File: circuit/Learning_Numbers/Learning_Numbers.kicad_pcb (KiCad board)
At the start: 2 copper layers, 141 x 123.3 mm, 109 parts, among them SW1 SW_DIP_x01, SW10 SW_Push, SW11 SW_Push, SW12 SW_Push, SW13 SW_Push, SW14 SW_Push, SW15 SW_Push, SW16 SW_Push, SW17 SW_Push, SW18 SW_Push, SW19 SW_Push, SW2 SW_Push, SW20 SW_Push, SW21 SW_Push, SW22 SW_Push, SW23 SW_Push, SW3 SW_Push, SW4 SW_Push, SW5 SW_Push, SW6 SW_Push, SW7 SW_Push, SW8 SW_Push, SW9 SW_Push, U1 ATmega168PA-P, U2 74HC165, U3 74HC165, U4 74HC595, U5 74HC595, U6 74HC595, U7 74HC595, U8 74HC595, Y1 8Mhz

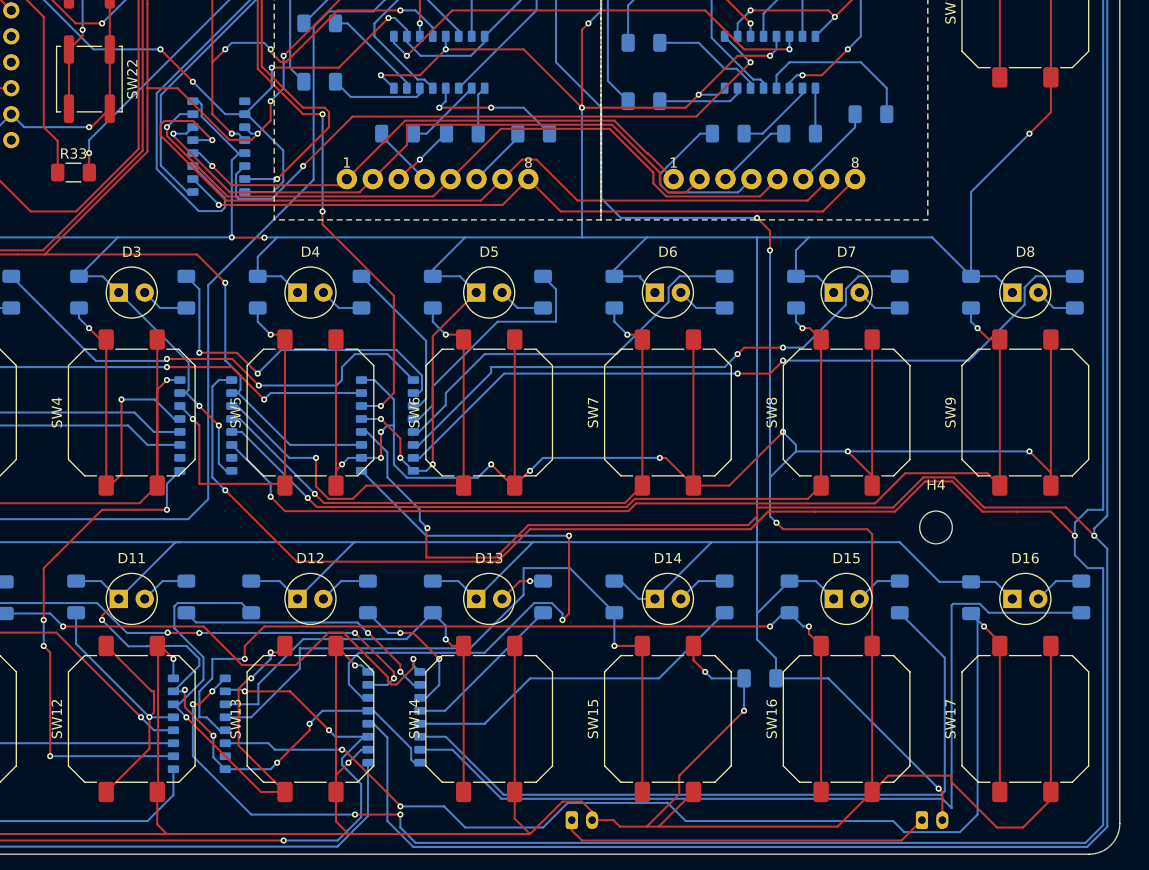
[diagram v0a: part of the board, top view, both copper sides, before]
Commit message: update pcb silk layer
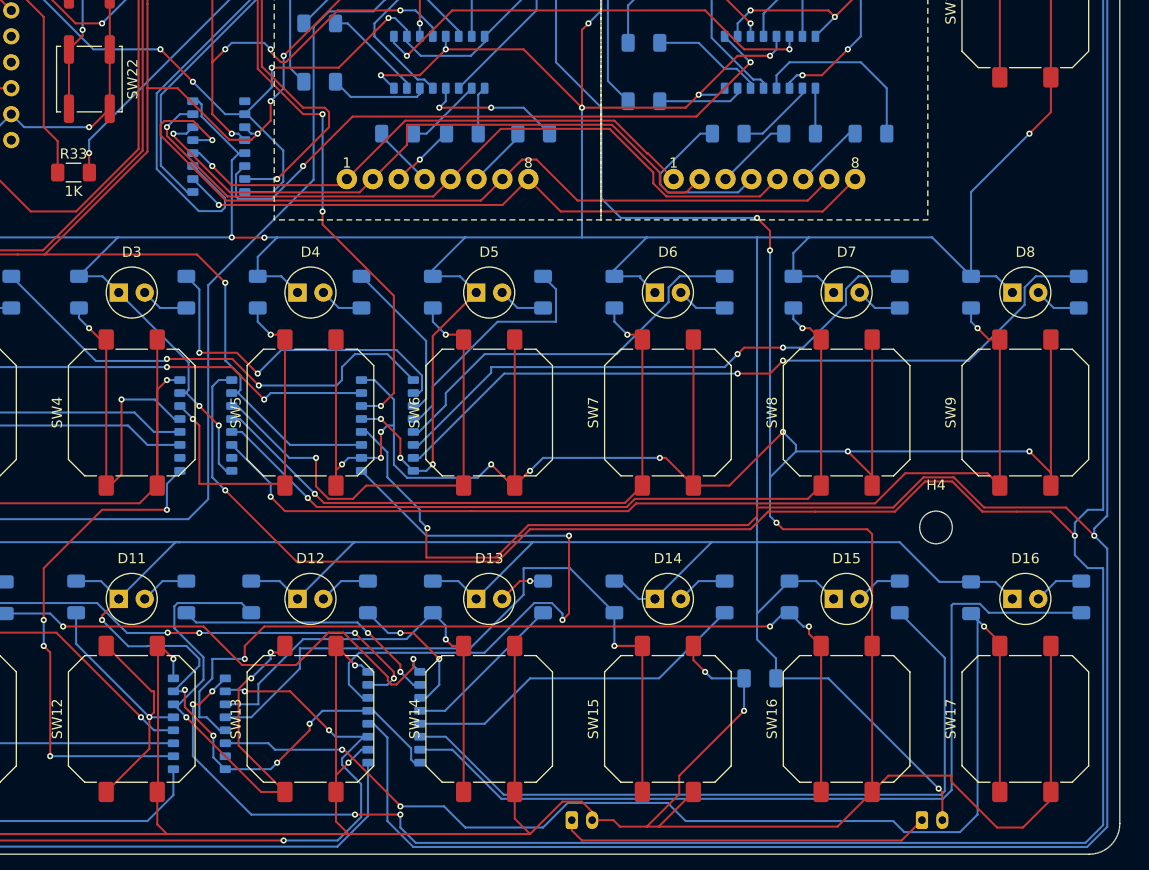
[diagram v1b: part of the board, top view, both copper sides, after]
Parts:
- SW1: value SW_DIP_x01 -> Power Switch
- moved R46 1.91 mm to (168.6, 91.4)
- moved R8 0.38 mm to (189.0, 107.0)
- moved R23 0.25 mm to (161.0, 107.0)
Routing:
- net col13: track 16.2 -> 18.1 mm
- net led16: track 87.4 -> 85.6 mm
- net Net-(R46-Pad2): track 8.46 -> 6.91 mm

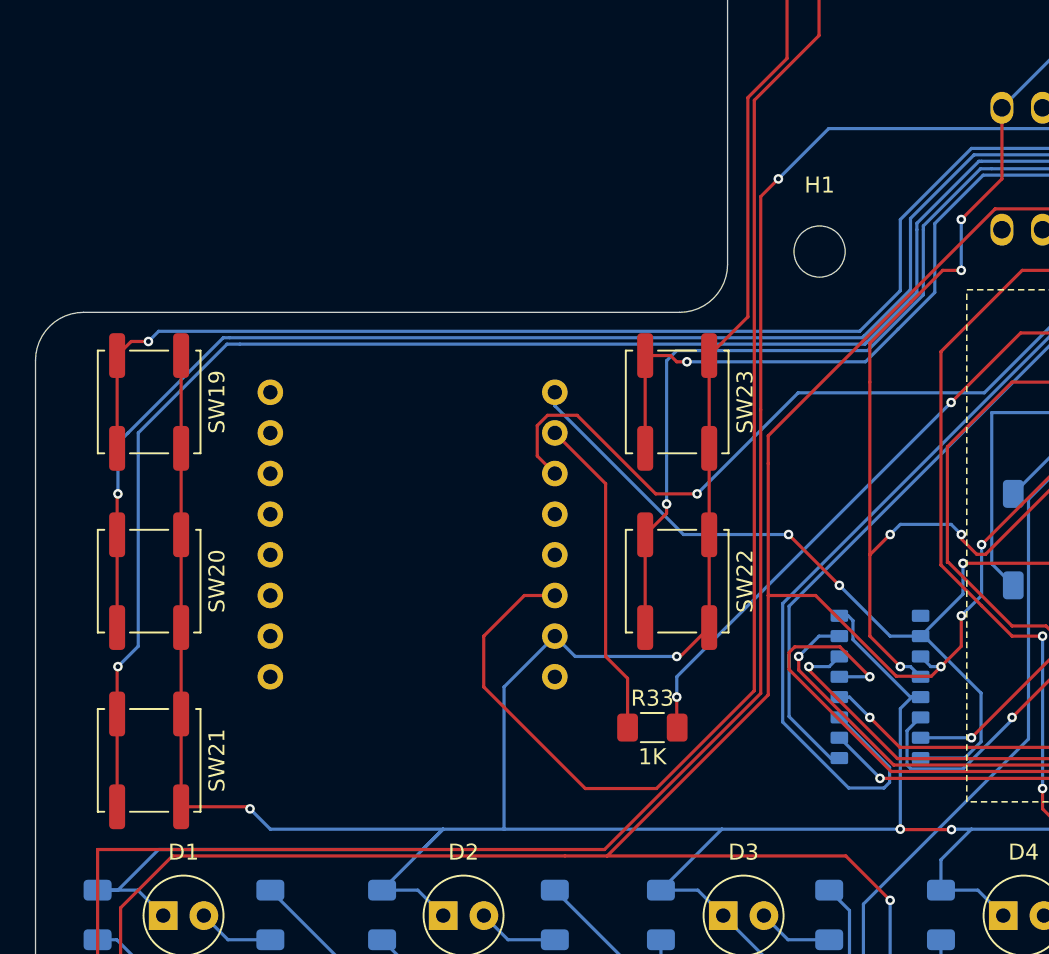
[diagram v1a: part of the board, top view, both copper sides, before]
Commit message: update circuit add capacitor DFPlayer and change speaker conections
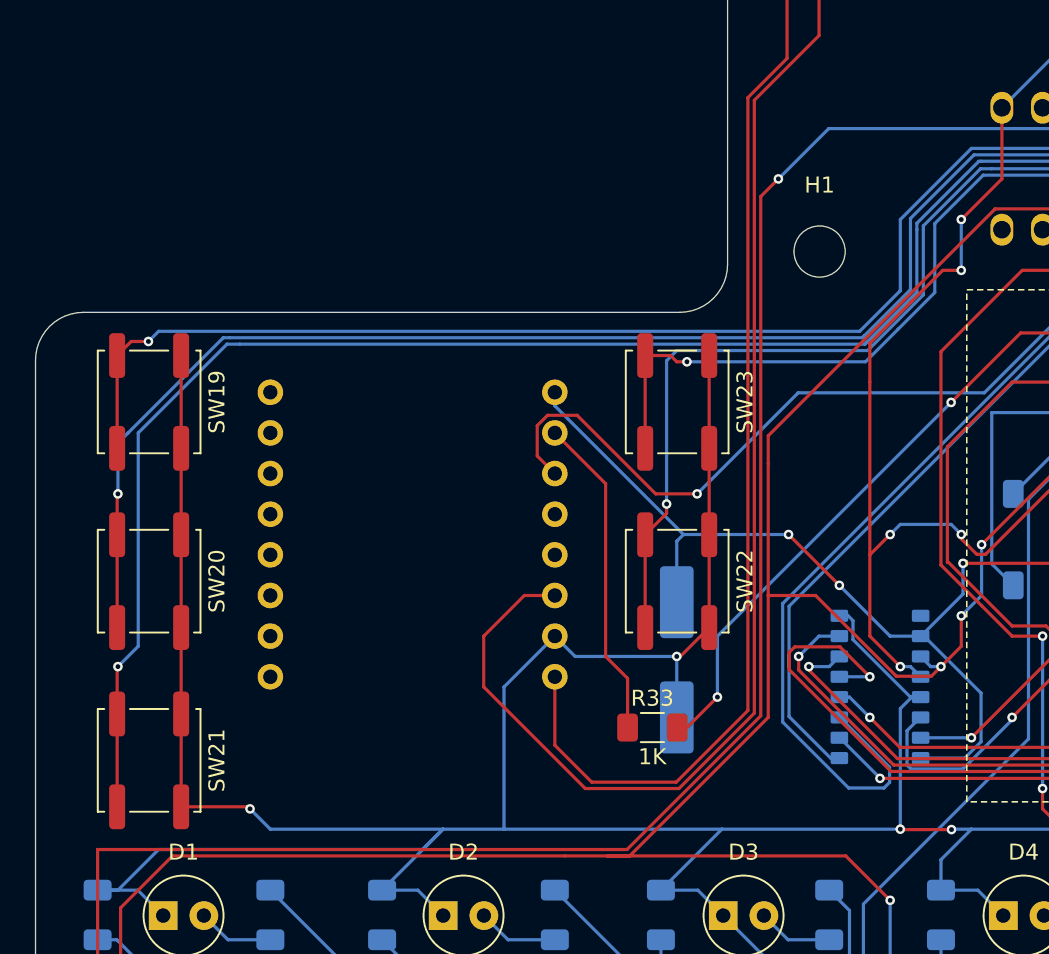
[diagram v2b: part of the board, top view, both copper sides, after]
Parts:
- added C4: 470uf, Capacitor_SMD:C_Elec_8x10.2, B.Cu at (92.1, 91.0)
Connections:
- LS1 pad 2: GND -> Net-(U11-SPK_2)
- U11 pad 8: unconnected-(U11-SPK_2-Pad8) -> Net-(U11-SPK_2)
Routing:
- net Net-(U11-SPK_2): track 0.00 -> 67.4 mm
- net GND: track 868.5 -> 845.2 mm
- net VCC: track 846.9 -> 851.3 mm
- net CLOCK: track 367.8 -> 368.6 mm
- net Net-(U11-SPK_1): track 78.4 -> 79.2 mm
- net Net-(U1-PB4): track 205.8 -> 206.6 mm

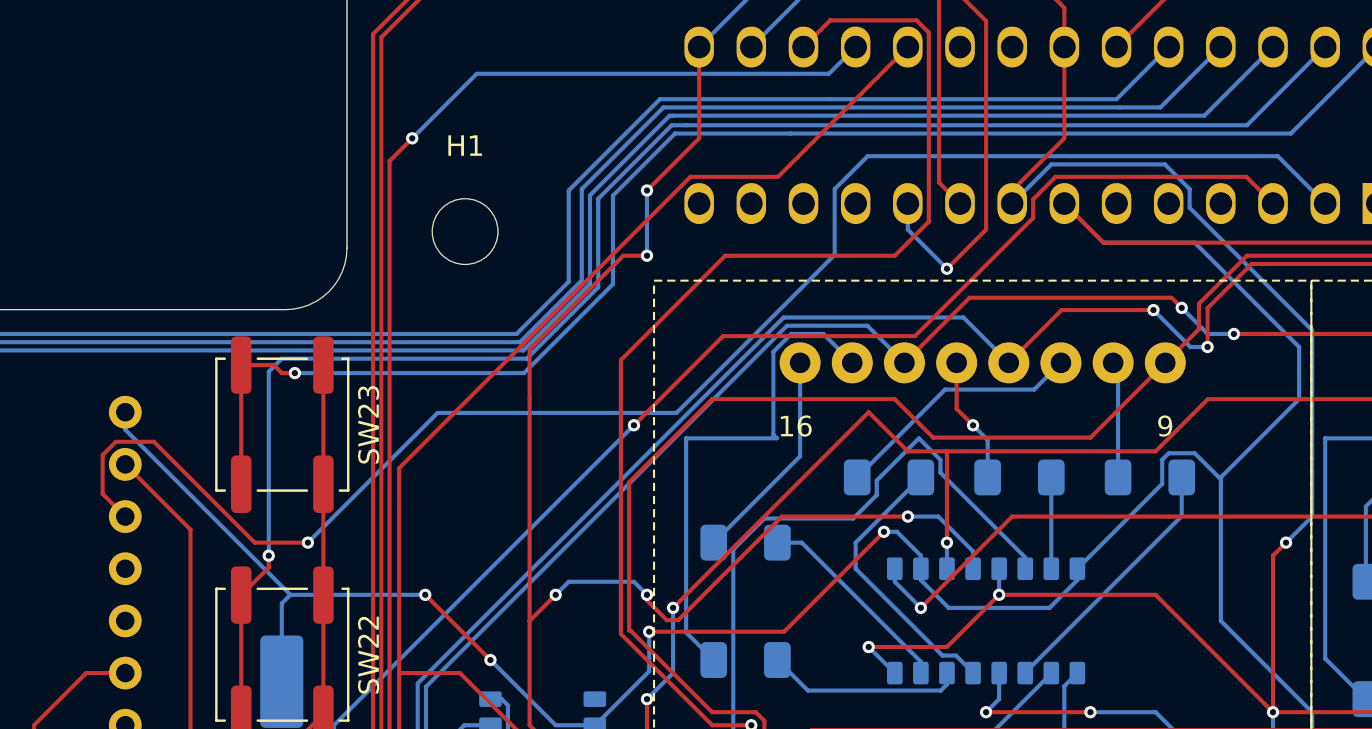
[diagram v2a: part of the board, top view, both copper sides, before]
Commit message: Update circuit to add DFPlayer 10 ohm resistor
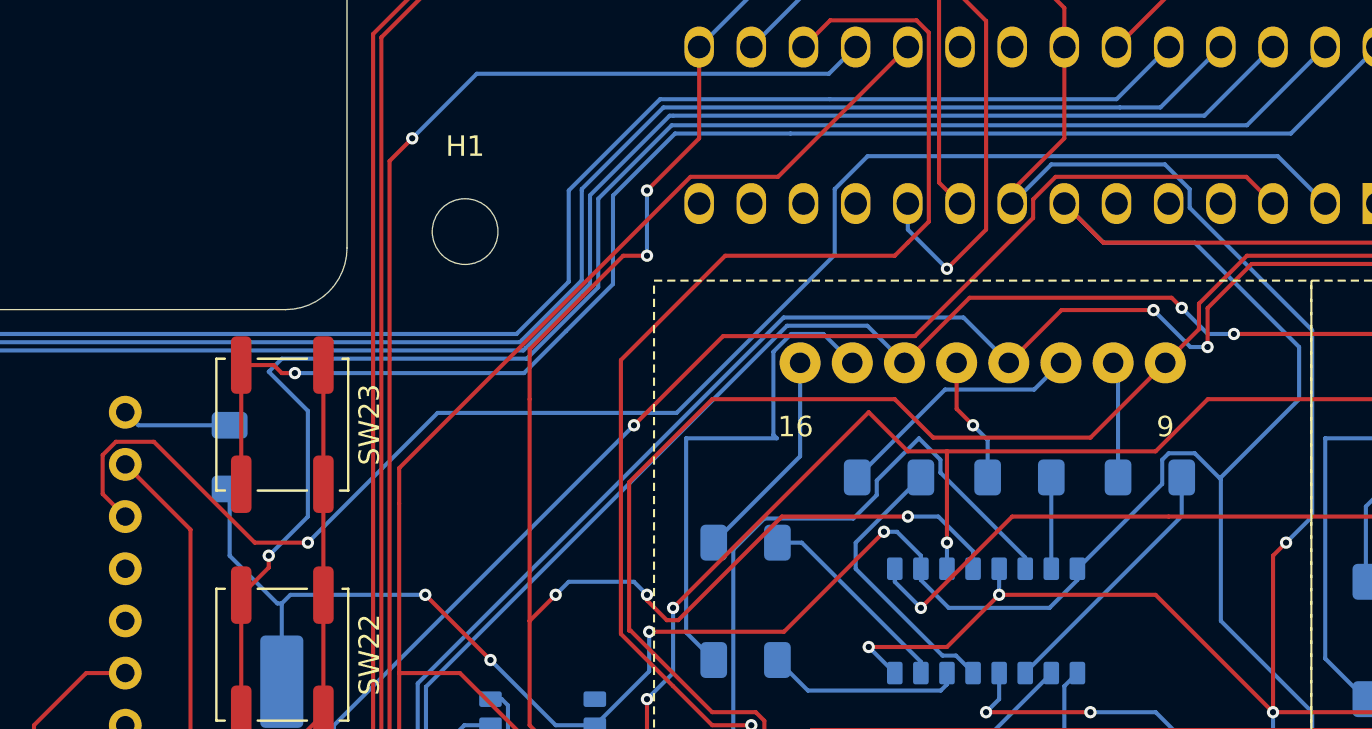
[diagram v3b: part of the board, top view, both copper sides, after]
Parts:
- added R50: 10R, Resistor_SMD:R_1206_3216Metric_Pad1.30x1.75mm_HandSolder, B.Cu at (89.5, 76.5)
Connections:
- U11 pad 1: VCC -> Net-(U11-VCC)
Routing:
- net VCC: track 851.3 -> 845.8 mm
- net Net-(U11-VCC): track 0.00 -> 5.34 mm
- net PC4: track 77.7 -> 79.3 mm
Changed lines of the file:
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@@
 	(net 137 "unconnected-(U11-DAC_R-Pad4)")
 	(net 138 "unconnected-(U11-USB+-Pad14)")
+	(net 139 "Net-(U11-VCC)")
 	(footprint "MountingHole:MountingHole_3.2mm_M3"
 		(layer "F.Cu")
@@
 		(embedded_fonts no)
 	)
+	(footprint "Resistor_SMD:R_1206_3216Metric_Pad1.30x1.75mm_HandSolder"
+		(layer "B.Cu")
+		(at 89.535 76.48 -90)
+		(descr "Resistor SMD 1206 (3216 Metric), square (rectangular) end terminal, IPC-7351 nominal with elongated pad for handsoldering. (Body size source: IPC-SM-782 page 72, https://www.pcb-3d.com/wordpress/wp-content/uploads/ipc-sm-782a_amendment_1_and_2.pdf), generated with kicad-footprint-generator")
+		(tags "resistor handsolder")
+		(property "Reference" "R50"
+			(at 0 1.83 90)
+			(layer "B.SilkS")
+			(effects
+				(font
+					(size 1 1)
+					(thickness 0.15)
+				)
+				(justify mirror)
+			)
+		)
+		(property "Value" "10R"
+			(at 0 -1.83 90)
+			(layer "B.SilkS")
+			(effects
+				(font
+					(size 1 1)
+					(thickness 0.15)
+				)
+				(justify mirror)
+			)
+		)
+		(property "Datasheet" "~"
+			(at 0 0 90)
+			(layer "B.Fab")
+			(hide yes)
+			(effects
+				(font
+					(size 1.27 1.27)
+					(thickness 0.15)
+				)
+				(justify mirror)
+			)
+		)
+		(property "Description" "Resistor"
+			(at 0 0 90)
+			(layer "B.Fab")
+			(hide yes)
+			(effects
+				(font
+					(size 1.27 1.27)
+					(thickness 0.15)
+				)
+				(justify mirror)
+			)
+		)
+		(property ki_fp_filters "R_*")
+		(sheetname "/")
+		(sheetfile "Learning_Numbers.kicad_sch")
+		(attr smd)
+		(fp_line
+			(start -0.727064 0.91)
+			(end 0.727064 0.91)
+			(stroke
+				(width 0.12)
+				(type solid)
+			)
+			(layer "B.SilkS")
+		)
+		(fp_line
+			(start -0.727064 -0.91)
+			(end 0.727064 -0.91)
+			(stroke
+				(width 0.12)
+				(type solid)
+			)
+			(layer "B.SilkS")
+		)
+		(fp_line
+			(start -2.45 1.13)
+			(end 2.45 1.13)
+			(stroke
+				(width 0.05)
+				(type solid)
+			)
+			(layer "B.CrtYd")
+		)
+		(fp_line
+			(start 2.45 1.13)
+			(end 2.45 -1.13)
+			(stroke
+				(width 0.05)
+				(type solid)
+			)
+			(layer "B.CrtYd")
+		)
+		(fp_line
+			(start -2.45 -1.13)
+			(end -2.45 1.13)
+			(stroke
+				(width 0.05)
+				(type solid)
+			)
+			(layer "B.CrtYd")
+		)
+		(fp_line
+			(start 2.45 -1.13)
+			(end -2.45 -1.13)
+			(stroke
+				(width 0.05)
+				(type solid)
+			)
+			(layer "B.CrtYd")
+		)
+		(fp_line
+			(start -1.6 0.8)
+			(end 1.6 0.8)
+			(stroke
+				(width 0.1)
+				(type solid)
+			)
+			(layer "B.Fab")
+		)
+		(fp_line
+			(start 1.6 0.8)
+			(end 1.6 -0.8)
+			(stroke
+				(width 0.1)
+				(type solid)
+			)
+			(layer "B.Fab")
+		)
+		(fp_line
+			(start -1.6 -0.8)
+			(end -1.6 0.8)
+			(stroke
+				(width 0.1)
+				(type solid)
+			)
+			(layer "B.Fab")
+		)
+		(fp_line
+			(start 1.6 -0.8)
+			(end -1.6 -0.8)
+			(stroke
+				(width 0.1)
+				(type solid)
+			)
+			(layer "B.Fab")
+		)
+		(fp_text user "${REFERENCE}"
+			(at 0 0 90)
+			(layer "B.Fab")
+			(effects
+				(font
+					(size 0.8 0.8)
+					(thickness 0.12)
+				)
+				(justify mirror)
+			)
+		)
+		(pad "1" smd roundrect
+			(at -1.55 0 270)
+			(size 1.3 1.75)
+			(layers "B.Cu" "B.Mask" "B.Paste")
+			(roundrect_rratio 0.192308)
+			(net 139 "Net-(U11-VCC)")
+			(pintype "passive")
+		)
+		(pad "2" smd roundrect
+			(at 1.55 0 270)
+			(size 1.3 1.75)
+			(layers "B.Cu" "B.Mask" "B.Paste")
+			(roundrect_rratio 0.192308)
+			(net 3 "VCC")
+			(pintype "passive")
+		)
+		(embedded_fonts no)
+		(model "${KICAD9_3DMODEL_DIR}/Resistor_SMD.3dshapes/R_1206_3216Metric.step"
+			(offset
+				(xyz 0 0 0)
+			)
+			(scale
+				(xyz 1 1 1)
+			)
+			(rotate
+				(xyz 0 0 0)
+			)
+		)
+	)
 	(footprint "SOP16:74HC595D"
 		(layer "B.Cu")
@@
 			(layers "*.Cu" "*.Mask")
 			(remove_unused_layers no)
-			(net 3 "VCC")
+			(net 139 "Net-(U11-VCC)")
 			(pinfunction "VCC")
 			(pintype "input")
@@
 	)
 	(segment
+		(start 91.860057 83.605057)
+		(end 89.535 81.28)
+		(width 0.2)
+		(layer "B.Cu")
+		(net 3)
+	)
+	(segment
 		(start 118.745 151.765)
 		(end 119.38 151.765)
@@
 	)
 	(segment
+		(start 89.535 81.28)
+		(end 89.535 78.03)
+		(width 0.2)
+		(layer "B.Cu")
+		(net 3)
+	)
+	(segment
 		(start 155.575 80.645)
 		(end 156.845 79.375)
@@
 	)
 	(segment
+		(start 92.075 83.605057)
+		(end 91.860057 83.605057)
+		(width 0.2)
+		(layer "B.Cu")
+		(net 3)
+	)
+	(segment
 		(start 142.24 97.79)
 		(end 142.24 88.9)
@@
 	)
 	(segment
-		(start 84.455 75.144943)
-		(end 84.455 74.295)
-		(width 0.2)
-		(layer "B.Cu")
-		(net 3)
-	)
-	(segment
 		(start 158.75 104.14)
 		(end 158.75 102.87)
@@
 	)
 	(segment
-		(start 92.495057 83.185)
-		(end 84.455 75.144943)
-		(width 0.2)
-		(layer "B.Cu")
-		(net 3)
-	)
-	(segment
 		(start 131.445 123.825)
 		(end 130.129 125.141)
@@
 	)
 	(segment
-		(start 91.44 72.323)
-		(end 91.44 81.28)
+		(start 139.065 60.325)
+		(end 111.0571 60.325)
 		(width 0.2)
 		(layer "B.Cu")
@@
 	)
 	(segment
-		(start 92.075 71.688)
-		(end 91.44 72.323)
+		(start 142.875 56.515)
+		(end 139.065 60.325)
 		(width 0.2)
 		(layer "B.Cu")
@@
 	)
 	(segment
-		(start 142.875 56.515)
-		(end 139.065 60.325)
+		(start 107.482 68.2093)
+		(end 104.0033 71.688)
 		(width 0.2)
 		(layer "B.Cu")
@@
 	)
 	(segment
-		(start 107.482 64.135)
-		(end 107.482 68.2093)
+		(start 92.075 71.688)
+		(end 91.44 72.323)
 		(width 0.2)
 		(layer "B.Cu")
@@
 	)
 	(segment
-		(start 111.76 60.325)
-		(end 111.0571 60.325)
+		(start 93.345 74.228)
+		(end 93.345 79.375)
 		(width 0.2)
 		(layer "B.Cu")
@@
 	)
 	(segment
-		(start 107.482 63.9001)
-		(end 107.482 64.135)
+		(start 91.44 72.323)
+		(end 93.345 74.228)
 		(width 0.2)
 		(layer "B.Cu")
@@
 	)
 	(segment
-		(start 111.0571 60.325)
-		(end 107.482 63.9001)
+		(start 104.0033 71.688)
+		(end 92.075 71.688)
 		(width 0.2)
 		(layer "B.Cu")
@@
 	)
 	(segment
-		(start 107.482 68.2093)
-		(end 104.0033 71.688)
+		(start 111.0571 60.325)
+		(end 107.482 63.9001)
 		(width 0.2)
 		(layer "B.Cu")
@@
 	)
 	(segment
-		(start 104.0033 71.688)
-		(end 92.075 71.688)
+		(start 107.482 63.9001)
+		(end 107.482 68.2093)
 		(width 0.2)
 		(layer "B.Cu")
@@
 	)
 	(segment
-		(start 139.065 60.325)
-		(end 111.76 60.325)
+		(start 93.345 79.375)
+		(end 91.44 81.28)
 		(width 0.2)
 		(layer "B.Cu")
@@
 		(net 132)
 	)
+	(segment
+		(start 89.535 74.93)
+		(end 85.09 74.93)
+		(width 0.2)
+		(layer "B.Cu")
+		(net 139)
+	)
+	(segment
+		(start 85.09 74.93)
+		(end 84.455 74.295)
+		(width 0.2)
+		(layer "B.Cu")
+		(net 139)
+	)
 	(zone
